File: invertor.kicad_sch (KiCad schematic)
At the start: 6 parts

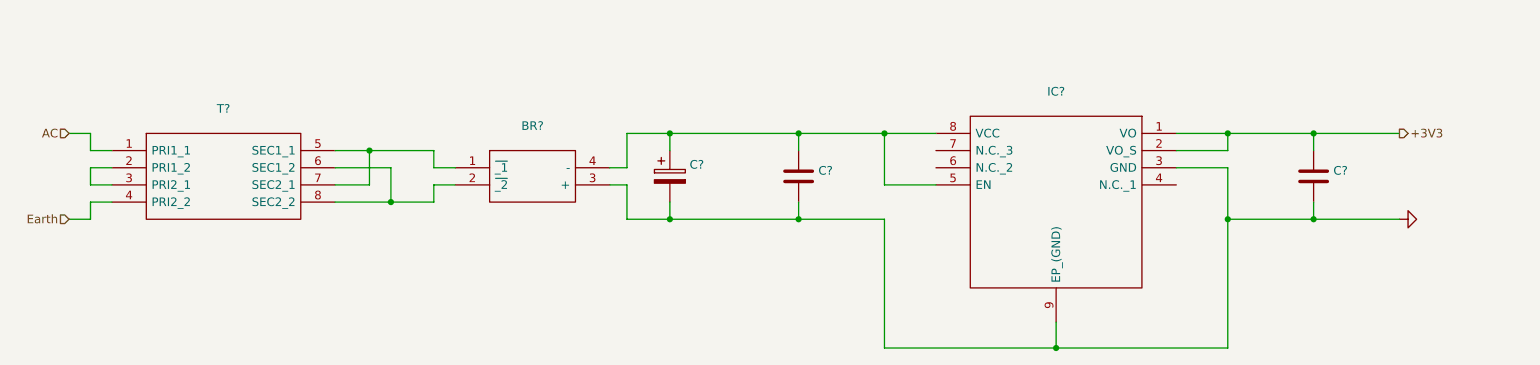
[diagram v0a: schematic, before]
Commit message: Added connectors
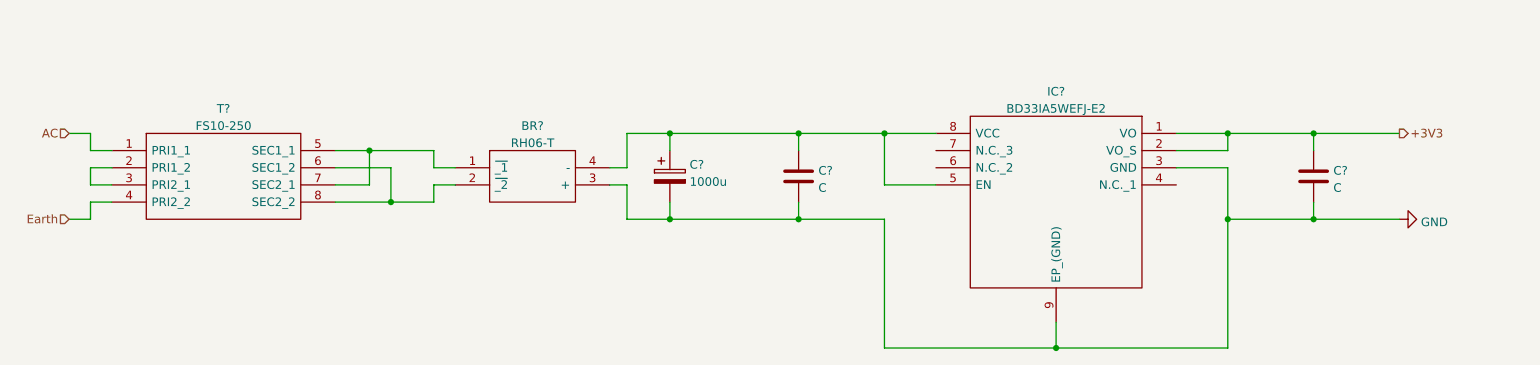
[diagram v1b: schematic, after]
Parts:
- BR?: value (none) -> RH06-T; footprint (none) -> SOP250P700X300-4N
- C?: value (none) -> 1000u
- C? (x2): value (none) -> C
- IC?: value (none) -> BD33IA5WEFJ-E2; footprint (none) -> SOIC127P600X100-9N
- T?: value (none) -> FS10-250; footprint (none) -> FS10250
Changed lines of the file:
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@@
       (effects (font (size 1.27 1.27)) hide)
     )
-    (property "Value" "" (id 1) (at 244.475 89.3338 90)
+    (property "Value" "GND" (id 1) (at 244.475 89.3338 90)
       (effects (font (size 1.27 1.27)) (justify right))
     )
@@
       (effects (font (size 1.27 1.27)) (justify left))
     )
-    (property "Value" "" (id 1) (at 136.271 83.3632 0)
+    (property "Value" "1000u" (id 1) (at 136.271 83.3632 0)
       (effects (font (size 1.27 1.27)) (justify left))
     )
@@
       (effects (font (size 1.27 1.27)) (justify left))
     )
-    (property "Value" "" (id 1) (at 231.521 84.2522 0)
+    (property "Value" "C" (id 1) (at 231.521 84.2522 0)
       (effects (font (size 1.27 1.27)) (justify left))
     )
@@
     (in_bom yes) (on_board yes) (fields_autoplaced)
     (property "Reference" "BR?" (id 0) (at 113.03 75.091 0))
-    (property "Value" "" (id 1) (at 113.03 77.6279 0))
-    (property "Footprint" "" (id 2) (at 120.65 78.74 0)
+    (property "Value" "RH06-T" (id 1) (at 113.03 77.6279 0))
+    (property "Footprint" "SOP250P700X300-4N" (id 2) (at 120.65 78.74 0)
       (effects (font (size 1.27 1.27)) (justify left) hide)
     )
@@
     (in_bom yes) (on_board yes) (fields_autoplaced)
     (property "Reference" "IC?" (id 0) (at 190.5 70.011 0))
-    (property "Value" "" (id 1) (at 190.5 72.5479 0))
-    (property "Footprint" "" (id 2) (at 176.53 73.66 0)
+    (property "Value" "BD33IA5WEFJ-E2" (id 1) (at 190.5 72.5479 0))
+    (property "Footprint" "SOIC127P600X100-9N" (id 2) (at 176.53 73.66 0)
       (effects (font (size 1.27 1.27)) (justify left) hide)
     )
@@
       (effects (font (size 1.27 1.27)) (justify left))
     )
-    (property "Value" "" (id 1) (at 155.321 84.2522 0)
+    (property "Value" "C" (id 1) (at 155.321 84.2522 0)
       (effects (font (size 1.27 1.27)) (justify left))
     )
@@
     (in_bom yes) (on_board yes) (fields_autoplaced)
     (property "Reference" "T?" (id 0) (at 67.31 72.551 0))
-    (property "Value" "" (id 1) (at 67.31 75.0879 0))
-    (property "Footprint" "" (id 2) (at 80.01 76.2 0)
+    (property "Value" "FS10-250" (id 1) (at 67.31 75.0879 0))
+    (property "Footprint" "FS10250" (id 2) (at 80.01 76.2 0)
       (effects (font (size 1.27 1.27)) (justify left) hide)
     )

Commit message: ERC
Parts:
- gave numbers to parts that had none: 6
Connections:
- net GND: now also BR401.4 (-); no longer BR401.3 (+)
- net at C401.1, C402.1, IC401.5 (EN)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: now also BR401.3 (+); no longer BR401.4 (-)
- net at T401.5 (SEC1_1), T401.7 (SEC2_1): now also BR401.2 (~{_2}); no longer BR401.1 (~{_1})
- net at T401.6 (SEC1_2), T401.8 (SEC2_2): now also BR401.1 (~{_1}); no longer BR401.2 (~{_2})
- net AC renamed IN.L
- net Earth renamed IN.N
- no-connect marks 0 -> 3

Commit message: Schematic cleanup
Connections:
- net 5V.N: now reaches BR401.1 (~{_1}), T401.6 (SEC1_2), T401.8 (SEC2_2)
- net 5V.L: now reaches BR401.2 (~{_2}), T401.5 (SEC1_1), T401.7 (SEC2_1)
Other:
- moved on the sheet: BR401, C401, C402, C403, IC401

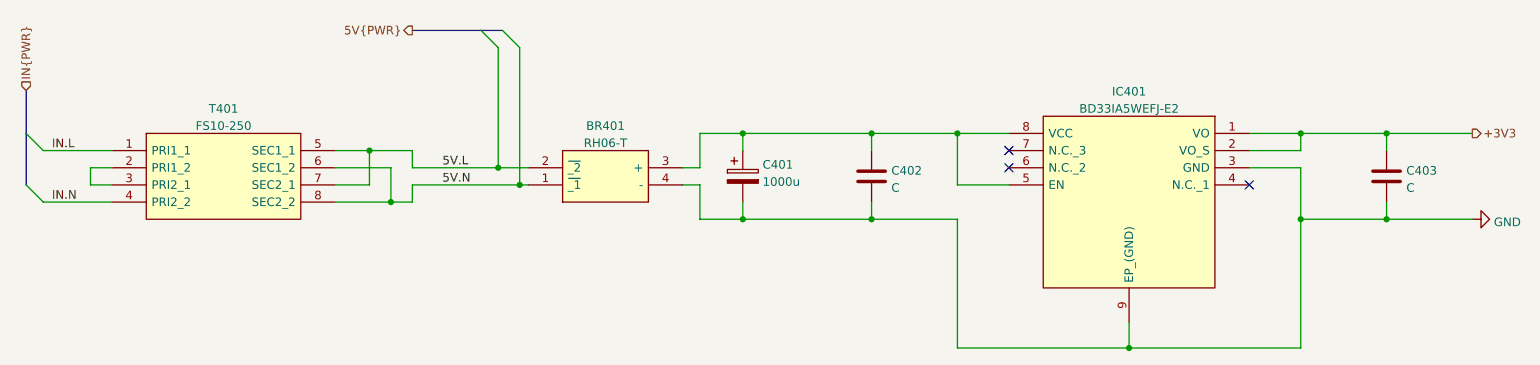
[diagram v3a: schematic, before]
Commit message: added zero detection
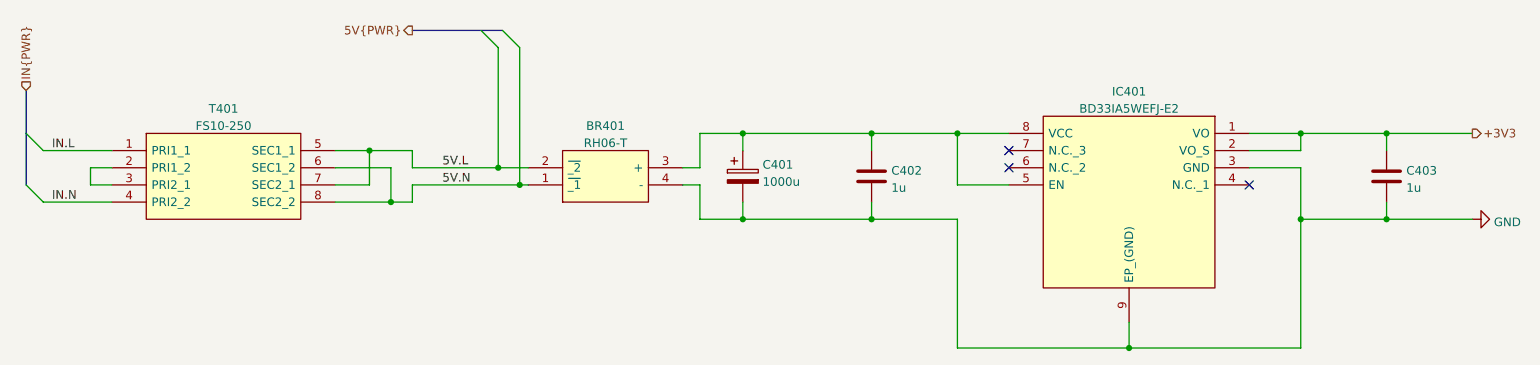
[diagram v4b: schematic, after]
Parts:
- C402, C403: value C -> 1u
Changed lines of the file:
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@@
       (effects (font (size 1.27 1.27)) (justify left))
     )
-    (property "Value" "C" (id 1) (at 242.316 84.2522 0)
+    (property "Value" "1u" (id 1) (at 242.316 84.2522 0)
       (effects (font (size 1.27 1.27)) (justify left))
     )
@@
       (effects (font (size 1.27 1.27)) (justify left))
     )
-    (property "Value" "C" (id 1) (at 166.116 84.2522 0)
+    (property "Value" "1u" (id 1) (at 166.116 84.2522 0)
       (effects (font (size 1.27 1.27)) (justify left))
     )
